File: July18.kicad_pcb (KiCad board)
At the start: 2 copper layers, 110 x 72.5 mm, 46 parts, among them CON1 BARREL_JACK, CON2 BARREL_JACK, P1 CONN_01X02, P2 CONN_01X02, Q1 SFH3711, Q10 SFH3711, Q11 SFH3711, Q12 SFH3711, Q13 SFH3711, Q14 SFH3711, Q15 SFH3711, Q16 Q_NMOS_GSD, Q2 SFH3711, Q3 SFH3711, Q4 SFH3711, Q5 SFH3711, Q6 SFH3711, Q7 SFH3711, Q8 SFH3711, Q9 SFH3711, U1 Teensy_3.1, U2 LM358, U3 CD74HC4067, U4 CL520

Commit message: Silkscreening
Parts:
- <-- HeaterPwr: renamed from CON1
- HeaterPwr -->: renamed from CON2
- LED Out: renamed from P2
- renumbered REF** to ?, P1 to TempProbe
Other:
- board text added: "3.3v"
- board text added: "Gnd"
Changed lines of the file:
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@@
     (area 137.449999 52.449999 247.550001 125.050001)
     (thickness 1.6)
-    (drawings 7)
+    (drawings 9)
     (tracks 316)
     (zones 0)
@@
     (descr "DC Barrel Jack")
     (tags "Power Jack")
-    (fp_text reference CON1 (at 10.09904 0 90) (layer F.SilkS)
-      (effects (font (size 1 1) (thickness 0.15)))
+    (fp_text reference "<-- HeaterPwr" (at 2.25 -3.5) (layer B.SilkS)
+      (effects (font (size 1 1) (thickness 0.15)) (justify mirror))
     )
     (fp_text value BARREL_JACK (at 0 -5.99948) (layer F.Fab)
@@
     (descr "DC Barrel Jack")
     (tags "Power Jack")
-    (fp_text reference CON2 (at 10.09904 0 90) (layer F.SilkS)
-      (effects (font (size 1 1) (thickness 0.15)))
+    (fp_text reference "HeaterPwr -->" (at 2 7.75) (layer B.SilkS)
+      (effects (font (size 1 1) (thickness 0.15)) (justify mirror))
     )
     (fp_text value BARREL_JACK (at 0 -5.99948) (layer F.Fab)
@@
     (descr "Through hole pin header")
     (tags "pin header")
-    (fp_text reference P2 (at 0 -5.1 180) (layer F.SilkS)
-      (effects (font (size 1 1) (thickness 0.15)))
+    (fp_text reference "LED Out" (at 0.5 5 180) (layer B.SilkS)
+      (effects (font (size 1 1) (thickness 0.15)) (justify mirror))
     )
     (fp_text value CONN_01X02 (at 0 -3.1 180) (layer F.Fab)
@@
     (descr "Through hole pin header")
     (tags "pin header")
-    (fp_text reference P1 (at 0 -5.1 180) (layer F.SilkS)
-      (effects (font (size 1 1) (thickness 0.15)))
+    (fp_text reference TempProbe (at 0.5 -3 180) (layer B.SilkS)
+      (effects (font (size 1 1) (thickness 0.15)) (justify mirror))
     )
     (fp_text value CONN_01X02 (at 0 -3.1 180) (layer F.Fab)
@@
     (descr "Mounting Hole 3.2mm, M3, DIN965")
     (tags "mounting hole 3.2mm m3 din965")
-    (fp_text reference REF** (at 0 -3.8) (layer F.SilkS)
+    (fp_text reference "" (at 0 -3.8) (layer F.SilkS)
       (effects (font (size 1 1) (thickness 0.15)))
     )
@@
     (descr "Mounting Hole 3.2mm, M3, DIN965")
     (tags "mounting hole 3.2mm m3 din965")
-    (fp_text reference REF** (at 0 -3.8) (layer F.SilkS)
+    (fp_text reference "" (at 0 -3.8) (layer F.SilkS)
       (effects (font (size 1 1) (thickness 0.15)))
     )
@@
     (descr "Mounting Hole 3.2mm, M3, DIN965")
     (tags "mounting hole 3.2mm m3 din965")
-    (fp_text reference REF** (at 0 -3.8) (layer F.SilkS)
+    (fp_text reference "" (at 0 -3.8) (layer F.SilkS)
       (effects (font (size 1 1) (thickness 0.15)))
     )
@@
     (descr "Mounting Hole 3.2mm, M3, DIN965")
     (tags "mounting hole 3.2mm m3 din965")
-    (fp_text reference REF** (at 0 -3.8) (layer F.SilkS)
+    (fp_text reference "" (at 0 -3.8) (layer F.SilkS)
       (effects (font (size 1 1) (thickness 0.15)))
     )
@@
       (xy -3.463683 0.979714) (xy -2.866571 0.379484)) (layer B.SilkS) (width 0.01))
   )
+  (gr_text 3.3v (at 145.75 115) (layer B.SilkS)
+    (effects (font (size 1 1) (thickness 0.25)) (justify mirror))
+  )
+  (gr_text Gnd (at 146 106) (layer B.SilkS)
+    (effects (font (size 1 1) (thickness 0.25)) (justify mirror))
+  )
   (dimension 72.5 (width 0.3) (layer F.Fab)

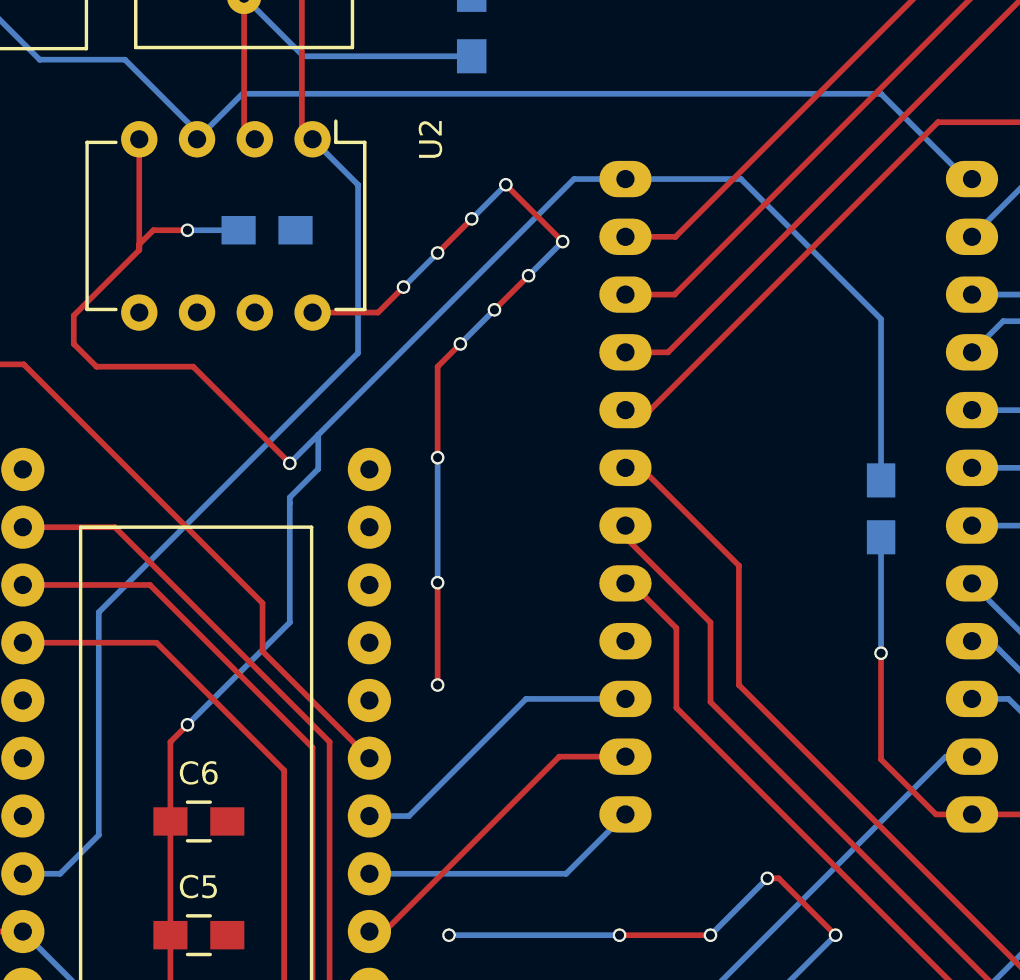
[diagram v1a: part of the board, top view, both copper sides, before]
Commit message: More via stitching, more bypass for mux
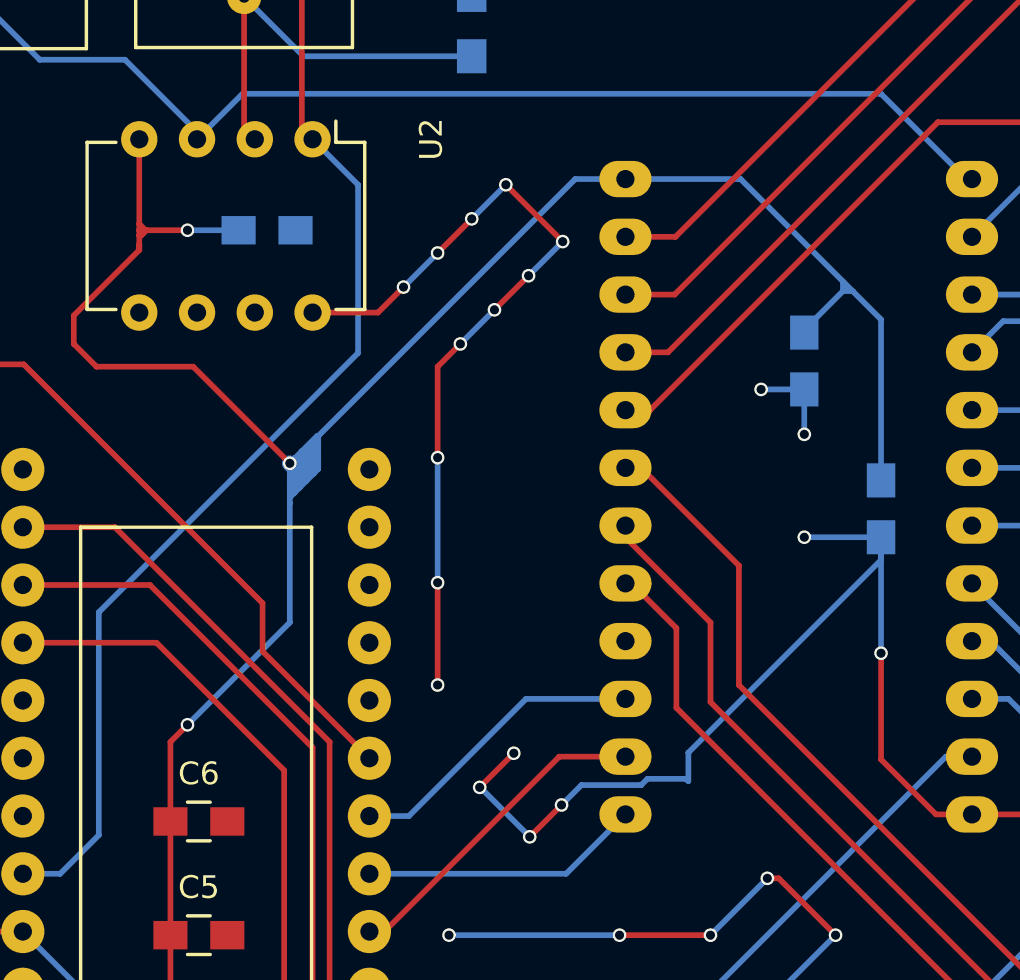
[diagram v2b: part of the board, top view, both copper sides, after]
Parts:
- added C7: 22nF, Capacitors_SMD:C_0805_HandSoldering, B.Cu at (191.6, 79.8)
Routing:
- net GND: track 197.5 -> 232.3 mm, vias 35 -> 42
- net +3V3: track 238.8 -> 256.5 mm

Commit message: MountHoles
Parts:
- added REF**: MountingHole_2.2mm_M2_ISO14580_Pad, Mounting_Holes:MountingHole_2.2mm_M2_ISO14580_Pad, F.Cu at (209.0, 122.0)
- added REF**: MountingHole_2.2mm_M2_ISO14580_Pad, Mounting_Holes:MountingHole_2.2mm_M2_ISO14580_Pad, F.Cu at (243.0, 122.0)
- added REF**: MountingHole_2.2mm_M2_ISO14580_Pad, Mounting_Holes:MountingHole_2.2mm_M2_ISO14580_Pad, F.Cu at (243.0, 60.0)
- added REF**: MountingHole_2.2mm_M2_ISO14580_Pad, Mounting_Holes:MountingHole_2.2mm_M2_ISO14580_Pad, F.Cu at (209.0, 60.0)
- moved R3 25.8 mm to (168.6, 139.3)
- moved R5 24.7 mm to (197.5, 138.8)
- moved R4 24.0 mm to (181.0, 138.7)
- moved D1 21.3 mm to (175.3, 139.4)
- moved D2 20.8 mm to (188.9, 139.0)
- moved D3 20.4 mm to (203.5, 136.9)
- moved ? 16.4 mm to (186.0, 120.0)
- moved TempProbe 6.70 mm to (142.3, 121.7)
- moved ? 5.51 mm to (149.0, 58.0)
- moved ? 1.00 mm to (149.0, 120.0)
- moved ? 0.35 mm to (186.0, 58.0)
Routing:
- net +3V3: track 256.5 -> 157.5 mm
- net Net-(D3-Pad2): track 63.7 -> 0.00 mm
- net Net-(D2-Pad2): track 57.8 -> 0.00 mm
- net Net-(D1-Pad2): track 50.1 -> 0.00 mm
- net TEMP_S: track 35.4 -> 17.5 mm
- net GND: track 232.3 -> 224.7 mm, vias 42 -> 40
- net Net-(D2-Pad1): track 5.98 -> 0.00 mm
- net Net-(D3-Pad1): track 3.90 -> 0.00 mm
- net Net-(D1-Pad1): track 3.56 -> 0.00 mm

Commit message: Blarg, KiCAD crashed, redoing all before, repushing often
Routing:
- net +3V3: track 157.5 -> 254.9 mm
- net /Phototransistors/S10: track 133.1 -> 65.9 mm, vias 1 -> 2
- net /Phototransistors/S9: track 126.2 -> 68.4 mm, vias 1 -> 2
- net /Phototransistors/S13: track 83.9 -> 97.0 mm
- net /Phototransistors/S14: track 79.4 -> 83.8 mm
- net /Phototransistors/S11: track 61.8 -> 58.4 mm
- net GND: track 224.7 -> 225.8 mm
- net /Phototransistors/S15: track 70.1 -> 71.0 mm
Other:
- board size 110 x 72.5 mm -> 110 x 73.8 mm

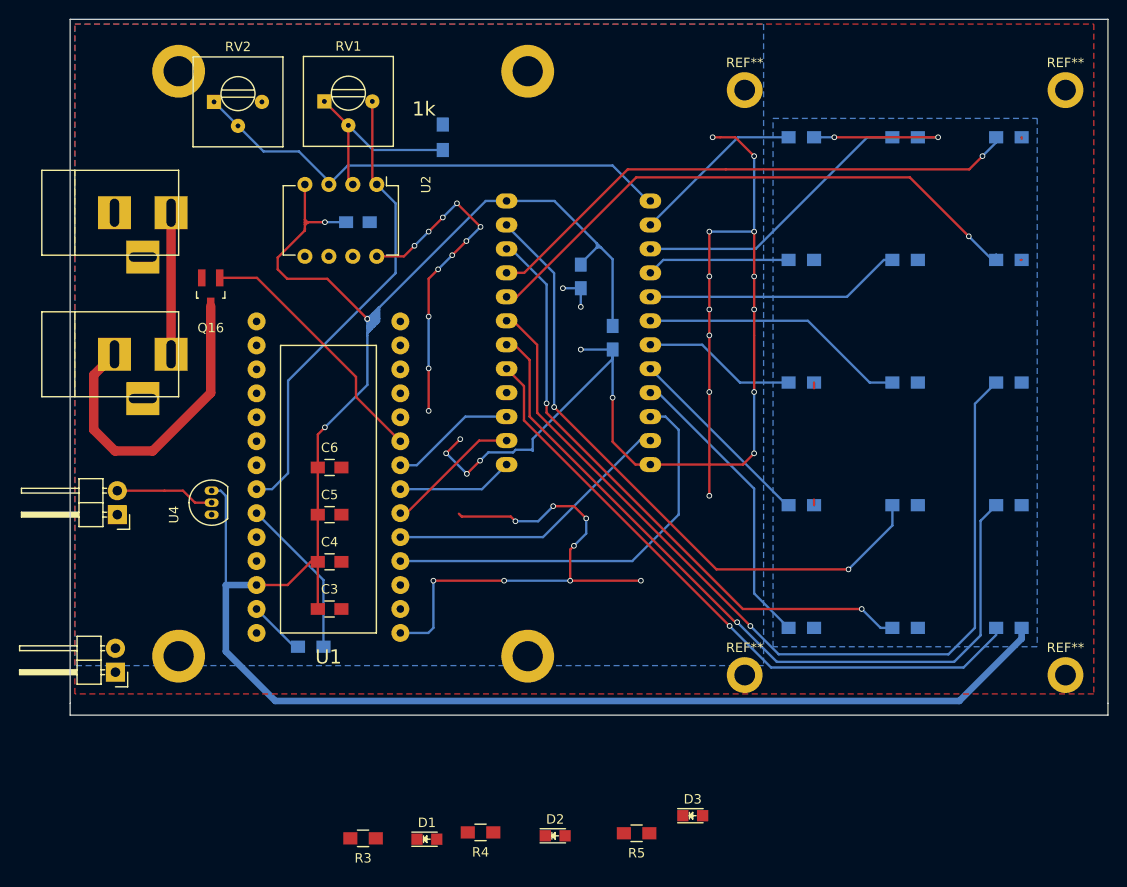
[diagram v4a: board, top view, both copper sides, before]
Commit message: Big revamp
Added mosfet to LED output
Changed LED driver to NCR405U

Changed phototransistor array to be 9mm * 9mm to match standard 96 well
sizing

Added 5v Linear reg to feed the teensy as well as a jumper so we can do
initial tests using usb power
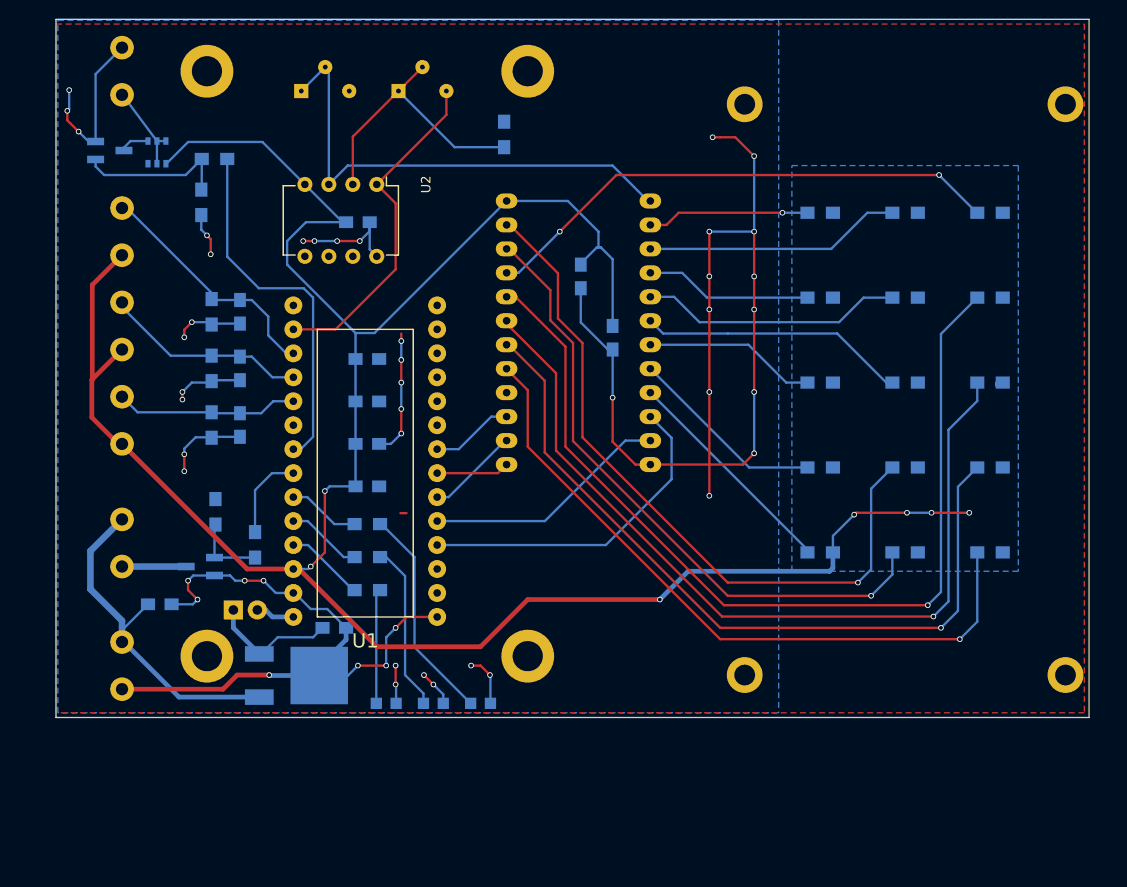
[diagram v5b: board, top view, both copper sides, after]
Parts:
- removed <-- HeaterPwr: BARREL_JACK, Connect:BARREL_JACK
- removed HeaterPwr -->: BARREL_JACK, Connect:BARREL_JACK
- removed LED Out: CONN_01X02, Pin_Headers:Pin_Header_Angled_1x02
- removed TempProbe: CONN_01X02, Pin_Headers:Pin_Header_Angled_1x02
- added C10: C, Capacitors_SMD:C_0805_HandSoldering, B.Cu at (155.5, 89.5)
- added C11: C, Capacitors_SMD:C_0805_HandSoldering, B.Cu at (155.5, 95.5)
- added C12: C, Capacitors_SMD:C_0805_HandSoldering, B.Cu at (155.5, 83.5)
- added C8: 100nF, Capacitors_SMD:C_0805_HandSoldering, B.Cu at (147.0, 114.5)
- added C9: 100nF, Capacitors_SMD:C_0805_HandSoldering, B.Cu at (165.5, 117.0)
- added P1: 12v In, CustomConnect:2_5mm_screw_terminal, B.Cu at (143.0, 121.0)
- added P2: HeatOut, CustomConnect:2_5mm_screw_terminal, B.Cu at (143.0, 108.0)
- added P3: LED, CustomConnect:2_5mm_screw_terminal, B.Cu at (143.0, 58.0)
- added P4: Temp1, CustomConnect:2_5mm_screw_terminal, B.Cu at (143.0, 75.0)
- added P5: Temp2, CustomConnect:2_5mm_screw_terminal, B.Cu at (143.0, 85.0)
- added P6: Temp3, CustomConnect:2_5mm_screw_terminal, B.Cu at (143.0, 95.0)
- added P7: ExtPwr, Pin_Headers:Pin_Header_Straight_1x02, B.Cu at (154.8, 115.1)
- added Q17: Q_NMOS_GSD, TO_SOT_Packages_SMD:SOT-23_Handsoldering, B.Cu at (141.7, 66.4)
- added R10: 1K, Resistors_SMD:R_0805_HandSoldering, B.Cu at (152.8, 67.3)
- added R11: 100K, Resistors_SMD:R_0805_HandSoldering, B.Cu at (151.4, 71.9)
- added R6: 1K, Resistors_SMD:R_0805_HandSoldering, B.Cu at (157.1, 108.2)
- added R7: 100K, Resistors_SMD:R_0805_HandSoldering, B.Cu at (152.9, 104.7)
- added R8: 6.8K, Resistors_SMD:R_0805_HandSoldering, B.Cu at (152.5, 89.5)
- added R9: 6.8K, Resistors_SMD:R_0805_HandSoldering, B.Cu at (152.5, 95.5)
- added U5: NCR405U, modules:SOT457, B.Cu at (146.7, 66.6)
- C3, C4, C5, C6, D1, D2, D3, Q16, R3, R4, R5, RV1, RV2: moved to B.Cu
- C7: value 22nF -> 22uF
- U4: value CL520 -> MC78M05CDT; footprint TO_SOT_Packages_THT:TO-92_Inline_Narrow_Oval -> TO_SOT_Packages_SMD:TO-252-2Lead; moved to B.Cu
- moved R5 40.9 mm to (169.0, 109.5), turned to 0 degrees
- moved R2 37.0 mm to (152.5, 83.5), turned to 270 degrees
- moved D3 34.6 mm to (171.0, 125.0), turned to 180 degrees
- moved R3 33.3 mm to (169.0, 106.0), turned to 0 degrees
- moved Q16 29.1 mm to (151.3, 110.5), turned to 270 degrees
- moved R4 28.3 mm to (169.0, 113.0), turned to 0 degrees
- moved D2 19.1 mm to (176.0, 125.0), turned to 180 degrees
- moved U4 17.8 mm to (157.6, 122.0)
- moved D1 15.5 mm to (181.0, 125.0), turned to 180 degrees
- moved C3 13.6 mm to (169.0, 102.0)
- moved C4 13.1 mm to (169.0, 97.5)
- moved C5 12.6 mm to (169.0, 93.0)
- moved C6 12.2 mm to (169.0, 88.5)
- moved RV2 9.32 mm to (162.0, 60.1)
- moved Q1 8.25 mm to (217.0, 109.0)
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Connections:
- D1 pad 1: Net-(D1-Pad1) -> GND
- D2 pad 1: Net-(D2-Pad1) -> GND
- D3 pad 1: Net-(D3-Pad1) -> GND
- Q16 pad 1: HEAT -> Net-(Q16-Pad1)
- R2 pad 1: TEMP_S -> TEMP_S_ONE
- R3 pad 1: Net-(D1-Pad1) -> Net-(R3-Pad1)
- R3 pad 2: GND -> Net-(D1-Pad2)
- R4 pad 1: Net-(D2-Pad1) -> Net-(R4-Pad1)
- R4 pad 2: GND -> Net-(D3-Pad2)
- R5 pad 1: Net-(D3-Pad1) -> Net-(R5-Pad1)
- R5 pad 2: GND -> Net-(D2-Pad2)
- U1 pad 14: Net-(D1-Pad2) -> Net-(RV1-Pad3)
- U1 pad 15: Net-(D2-Pad2) -> TEMP_S_ONE
- U1 pad 16: Net-(D3-Pad2) -> TEMP_S_TWO
- U1 pad 17: Net-(U1-Pad17) -> TEMP_S_THREE
- U1 pad 19: Net-(U1-Pad19) -> LEDS
- U1 pad 20: Net-(RV1-Pad3) -> HEAT
- U1 pad 21: TEMP_S -> Net-(R3-Pad1)
- U1 pad 22: Net-(U1-Pad22) -> Net-(R5-Pad1)
- U1 pad 23: Net-(U1-Pad23) -> Net-(R4-Pad1)
- U1 pad 7: HEAT -> Net-(U1-Pad7)
- U4 pad 1: GND -> +12V
- U4 pad 2: Net-(P2-Pad2) -> GND
- U4 pad 3: +3V3 -> TeensyVin
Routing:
- net /Phototransistors/S12: track 61.9 -> 101.2 mm
- net LEDS: track 0.00 -> 38.6 mm
- net +12V: track 0.00 -> 37.9 mm
- net GND: track 225.8 -> 259.2 mm, vias 40 -> 47
- net Net-(P2-Pad1): track 34.0 -> 6.80 mm
- net TEMP_S_ONE: track 0.00 -> 26.1 mm
- net Net-(D1-Pad2): track 0.00 -> 23.1 mm
- net TEMP_S_TWO: track 0.00 -> 21.7 mm
- net TEMP_S_THREE: track 0.00 -> 20.1 mm
- net HEAT: track 27.6 -> 9.26 mm
- net Net-(D2-Pad2): track 0.00 -> 18.1 mm
- net TEMP_S: track 17.5 -> 0.00 mm
- net Net-(Q17-Pad1): track 0.00 -> 16.3 mm
- net HEATER_PWR: track 15.0 -> 0.00 mm
- net TeensyVin: track 0.00 -> 13.9 mm
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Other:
- board size 110 x 73.8 mm -> 109.5 x 74 mm
- board text removed: "1k"
- board text removed: "3.3v"
- board text removed: "Gnd"

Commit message: Added Name ^.^
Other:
- board text added: "LAMP Diagnostics"

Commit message: Moved via ^.^
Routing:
- net GND: track 259.2 -> 253.0 mm, vias 47 -> 45
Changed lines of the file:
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@@
     (thickness 1.6)
     (drawings 8)
-    (tracks 462)
+    (tracks 457)
     (zones 0)
     (modules 67)
@@
   (segment (start 195 77.925) (end 195 85) (width 0.25) (layer B.Cu) (net 1))
   (segment (start 235.65 91.35) (end 235.65 91) (width 0.25) (layer B.Cu) (net 1))
+  (segment (start 166.75 117) (end 166.8 117) (width 0.25) (layer B.Cu) (net 2) (status C00000))
+  (segment (start 166.8 117) (end 168.6 115.2) (width 0.25) (layer B.Cu) (net 2) (status 400000))
+  (segment (start 169.24 115.84) (end 176.4 115.84) (width 0.25) (layer F.Cu) (net 2) (status 800000))
+  (segment (start 168.6 115.2) (end 169.24 115.84) (width 0.25) (layer F.Cu) (net 2))
+  (via (at 168.6 115.2) (size 0.6) (drill 0.4) (layers F.Cu B.Cu) (net 2))
   (segment (start 143 123.5) (end 153.7 123.5) (width 0.5) (layer F.Cu) (net 2))
   (segment (start 158.65 122.05) (end 163.9 122.05) (width 0.5) (layer B.Cu) (net 2))
@@
   (segment (start 140.19886 65.45) (end 140.19886 58.30114) (width 0.25) (layer B.Cu) (net 2))
   (segment (start 140.19886 58.30114) (end 143 55.5) (width 0.25) (layer B.Cu) (net 2))
-  (segment (start 176.4 115.84) (end 173.16 115.84) (width 0.25) (layer F.Cu) (net 2))
-  (segment (start 166.95 122.05) (end 163.9 122.05) (width 0.25) (layer B.Cu) (net 2))
-  (segment (start 168 121) (end 166.95 122.05) (width 0.25) (layer B.Cu) (net 2))
-  (via (at 168 121) (size 0.6) (drill 0.4) (layers F.Cu B.Cu) (net 2))
-  (segment (start 171 121) (end 168 121) (width 0.25) (layer F.Cu) (net 2))
-  (via (at 171 121) (size 0.6) (drill 0.4) (layers F.Cu B.Cu) (net 2))
-  (segment (start 171 118) (end 171 121) (width 0.25) (layer B.Cu) (net 2))
-  (segment (start 172 117) (end 171 118) (width 0.25) (layer B.Cu) (net 2))
-  (via (at 172 117) (size 0.6) (drill 0.4) (layers F.Cu B.Cu) (net 2))
-  (segment (start 173.16 115.84) (end 172 117) (width 0.25) (layer F.Cu) (net 2))
   (segment (start 152.80114 111.45) (end 154.45 111.45) (width 0.25) (layer B.Cu) (net 2))
   (segment (start 159.3 113.3) (end 161.16 113.3) (width 0.25) (layer B.Cu) (net 2))
